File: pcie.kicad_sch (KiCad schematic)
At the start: 9 parts, among them U3 XC7K160T-FFG676

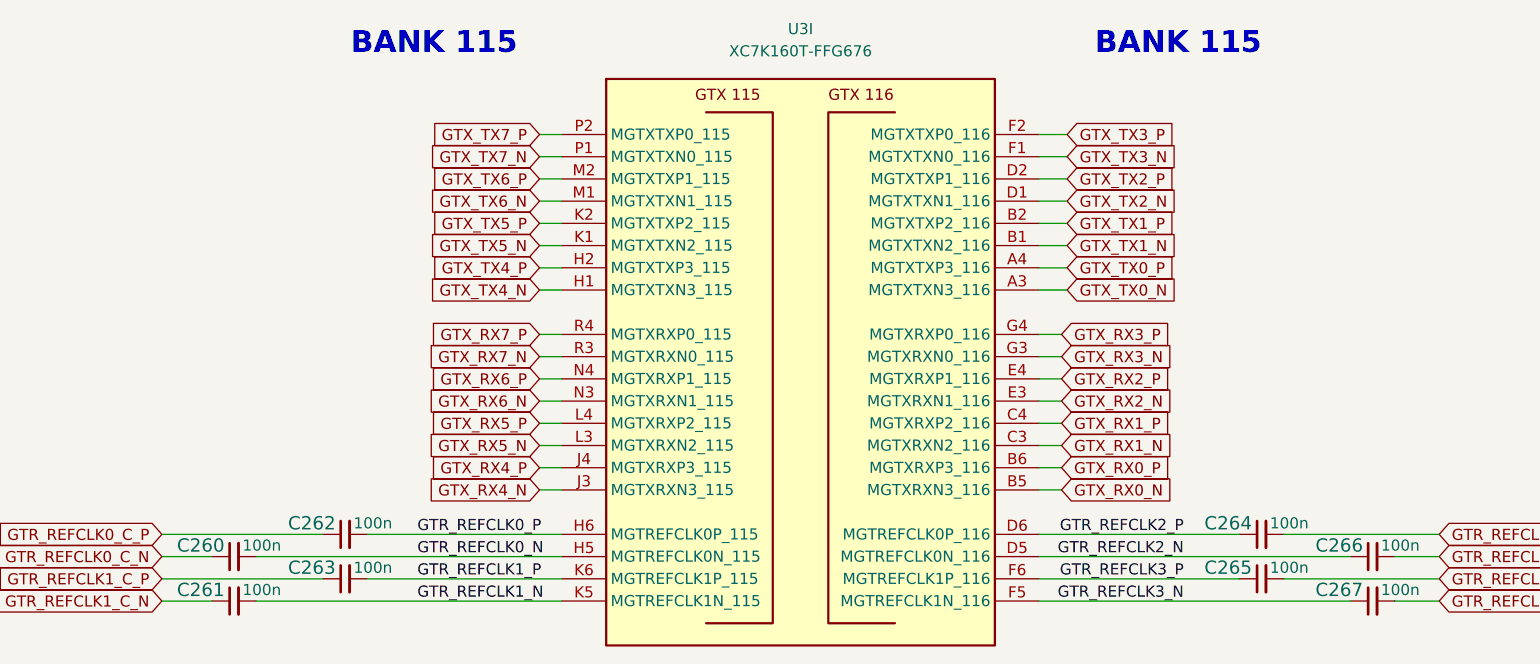
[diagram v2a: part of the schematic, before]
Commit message: Update designators and sync schematic with PCB
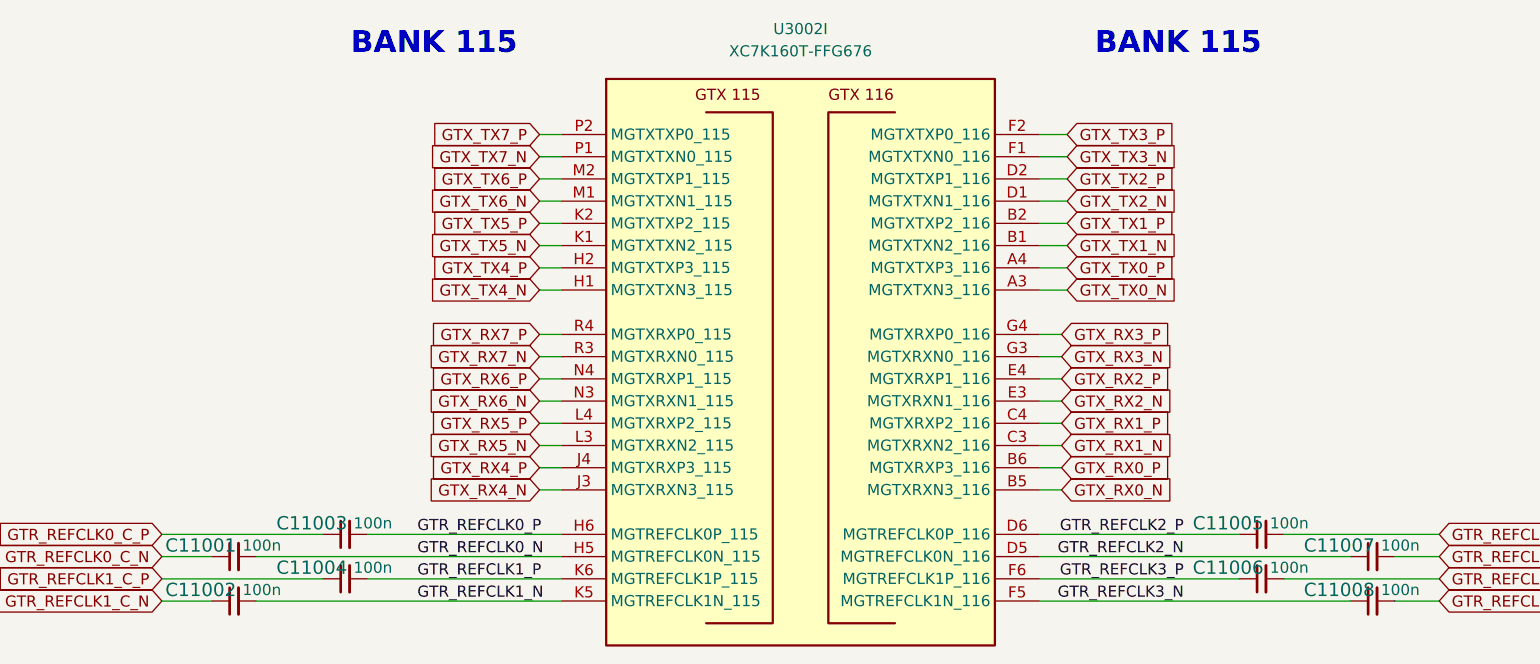
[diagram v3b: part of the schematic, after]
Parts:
- renumbered C260 to C11001, C261 to C11002, C262 to C11003, C263 to C11004, C264 to C11005, C265 to C11006, C266 to C11007, C267 to C11008, U3 to U3002
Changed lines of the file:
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@@
   (symbol (lib_id "data-center-rdimm-ddr4-tester:C_100n_0402") (at 144.78 99.06 0) (unit 1)
     (in_bom yes) (on_board yes)
-    (property "Reference" "C262" (id 0) (at 143.51 97.79 0)
+    (property "Reference" "C11003" (id 0) (at 143.51 97.79 0)
       (effects (font (size 1.524 1.524)))
     )
@@
   (symbol (lib_id "data-center-rdimm-ddr4-tester:C_100n_0402") (at 249.555 104.14 0) (mirror x) (unit 1)
     (in_bom yes) (on_board yes)
-    (property "Reference" "C265" (id 0) (at 248.285 102.87 0)
+    (property "Reference" "C11006" (id 0) (at 248.285 102.87 0)
       (effects (font (size 1.524 1.524)))
     )
@@
   (symbol (lib_id "data-center-rdimm-ddr4-tester:C_100n_0402") (at 132.08 106.68 0) (unit 1)
     (in_bom yes) (on_board yes)
-    (property "Reference" "C261" (id 0) (at 130.81 105.41 0)
+    (property "Reference" "C11002" (id 0) (at 130.81 105.41 0)
       (effects (font (size 1.524 1.524)))
     )
@@
   (symbol (lib_id "data-center-rdimm-ddr4-tester:C_100n_0402") (at 144.78 104.14 0) (unit 1)
     (in_bom yes) (on_board yes)
-    (property "Reference" "C263" (id 0) (at 143.51 102.87 0)
+    (property "Reference" "C11004" (id 0) (at 143.51 102.87 0)
       (effects (font (size 1.524 1.524)))
     )
@@
   (symbol (lib_id "data-center-rdimm-ddr4-tester:C_100n_0402") (at 262.255 101.6 0) (mirror x) (unit 1)
     (in_bom yes) (on_board yes)
-    (property "Reference" "C266" (id 0) (at 260.985 100.33 0)
+    (property "Reference" "C11007" (id 0) (at 260.985 100.33 0)
       (effects (font (size 1.524 1.524)))
     )
@@
   (symbol (lib_id "data-center-rdimm-ddr4-tester:XC7K160T-FFG676") (at 172.085 53.34 0) (unit 9)
     (in_bom yes) (on_board yes) (fields_autoplaced)
-    (property "Reference" "U3" (id 0) (at 199.39 41.275 0))
+    (property "Reference" "U3002" (id 0) (at 199.39 41.275 0))
     (property "Value" "XC7K160T-FFG676" (id 1) (at 199.39 43.815 0)
       (effects (font (size 1.27 1.27) (thickness 0.15)))
@@
   (symbol (lib_id "data-center-rdimm-ddr4-tester:C_100n_0402") (at 262.255 106.68 0) (mirror x) (unit 1)
     (in_bom yes) (on_board yes)
-    (property "Reference" "C267" (id 0) (at 260.985 105.41 0)
+    (property "Reference" "C11008" (id 0) (at 260.985 105.41 0)
       (effects (font (size 1.524 1.524)))
     )
@@
   (symbol (lib_id "data-center-rdimm-ddr4-tester:C_100n_0402") (at 132.08 101.6 0) (unit 1)
     (in_bom yes) (on_board yes)
-    (property "Reference" "C260" (id 0) (at 130.81 100.33 0)
+    (property "Reference" "C11001" (id 0) (at 130.81 100.33 0)
       (effects (font (size 1.524 1.524)))
     )
@@
   (symbol (lib_id "data-center-rdimm-ddr4-tester:C_100n_0402") (at 249.555 99.06 0) (mirror x) (unit 1)
     (in_bom yes) (on_board yes)
-    (property "Reference" "C264" (id 0) (at 248.285 97.79 0)
+    (property "Reference" "C11005" (id 0) (at 248.285 97.79 0)
       (effects (font (size 1.524 1.524)))
     )

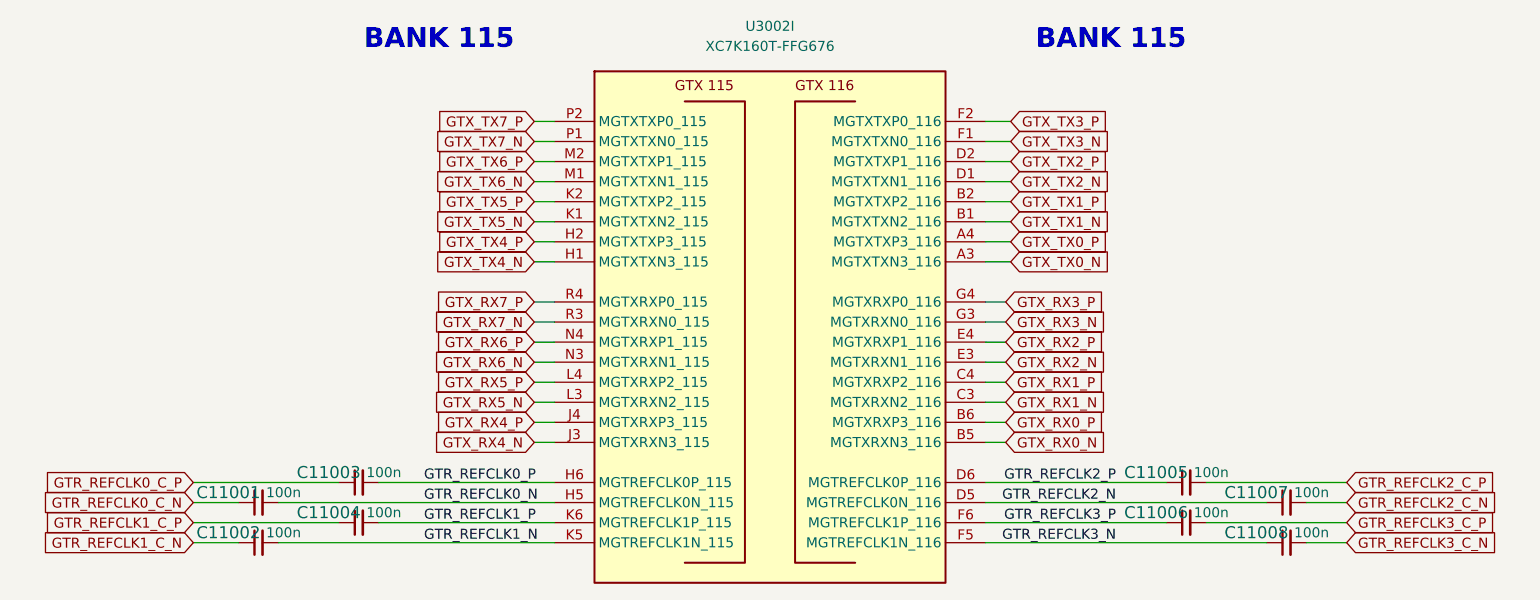
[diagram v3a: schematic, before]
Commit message: Update PCIe connection
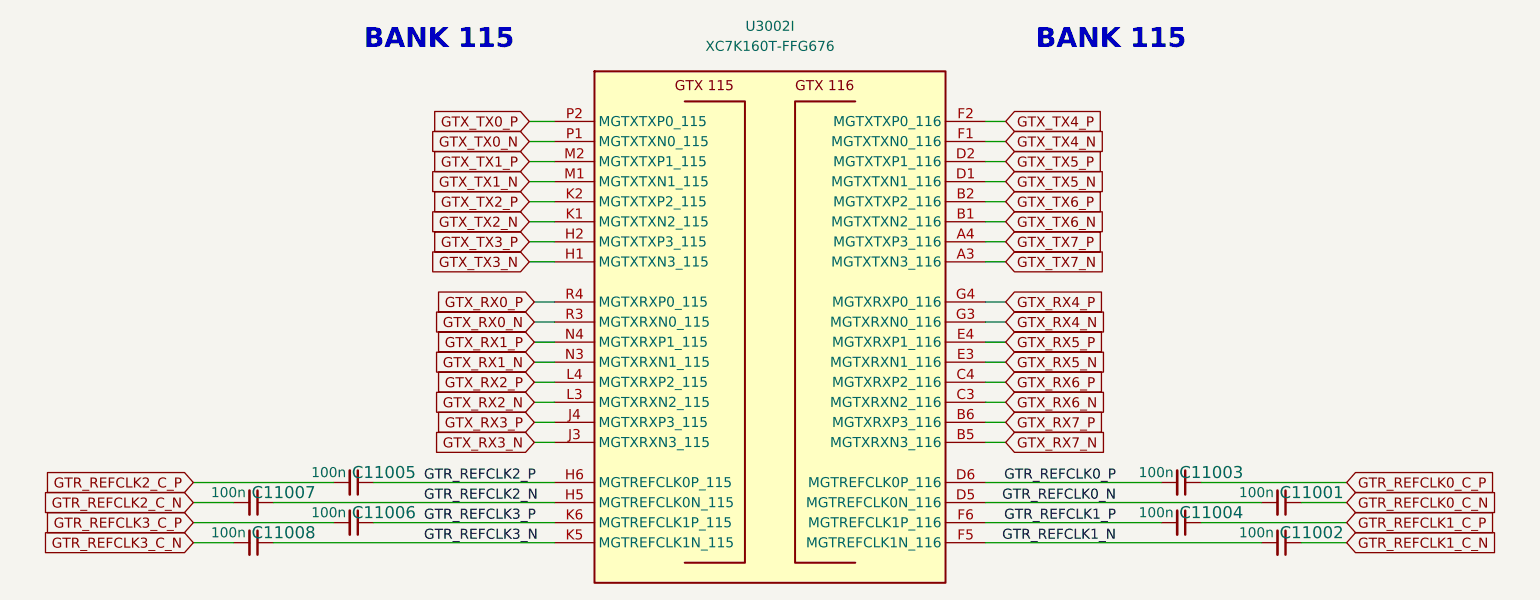
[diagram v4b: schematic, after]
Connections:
- net GTR_REFCLK0_N: now also U3002.D5 (MGTREFCLK0N_116); no longer U3002.H5 (MGTREFCLK0N_115)
- net GTR_REFCLK0_P: now also U3002.D6 (MGTREFCLK0P_116); no longer U3002.H6 (MGTREFCLK0P_115)
- net GTR_REFCLK1_N: now also U3002.F5 (MGTREFCLK1N_116); no longer U3002.K5 (MGTREFCLK1N_115)
- net GTR_REFCLK1_P: now also U3002.F6 (MGTREFCLK1P_116); no longer U3002.K6 (MGTREFCLK1P_115)
- net GTR_REFCLK2_N: now also U3002.H5 (MGTREFCLK0N_115); no longer U3002.D5 (MGTREFCLK0N_116)
- net GTR_REFCLK2_P: now also U3002.H6 (MGTREFCLK0P_115); no longer U3002.D6 (MGTREFCLK0P_116)
- net GTR_REFCLK3_N: now also U3002.K5 (MGTREFCLK1N_115); no longer U3002.F5 (MGTREFCLK1N_116)
- net GTR_REFCLK3_P: now also U3002.K6 (MGTREFCLK1P_115); no longer U3002.F6 (MGTREFCLK1P_116)
- net GTX_RX0_N: now also U3002.R3 (MGTXRXN0_115); no longer U3002.B5 (MGTXRXN3_116)
- net GTX_RX0_P: now also U3002.R4 (MGTXRXP0_115); no longer U3002.B6 (MGTXRXP3_116)
- net GTX_RX1_N: now also U3002.N3 (MGTXRXN1_115); no longer U3002.C3 (MGTXRXN2_116)
- net GTX_RX1_P: now also U3002.N4 (MGTXRXP1_115); no longer U3002.C4 (MGTXRXP2_116)
- net GTX_RX2_N: now also U3002.L3 (MGTXRXN2_115); no longer U3002.E3 (MGTXRXN1_116)
- net GTX_RX2_P: now also U3002.L4 (MGTXRXP2_115); no longer U3002.E4 (MGTXRXP1_116)
- net GTX_RX3_N: now also U3002.J3 (MGTXRXN3_115); no longer U3002.G3 (MGTXRXN0_116)
- net GTX_RX3_P: now also U3002.J4 (MGTXRXP3_115); no longer U3002.G4 (MGTXRXP0_116)
- net GTX_RX4_N: now also U3002.G3 (MGTXRXN0_116); no longer U3002.J3 (MGTXRXN3_115)
- net GTX_RX4_P: now also U3002.G4 (MGTXRXP0_116); no longer U3002.J4 (MGTXRXP3_115)
- net GTX_RX5_N: now also U3002.E3 (MGTXRXN1_116); no longer U3002.L3 (MGTXRXN2_115)
- net GTX_RX5_P: now also U3002.E4 (MGTXRXP1_116); no longer U3002.L4 (MGTXRXP2_115)
- net GTX_RX6_N: now also U3002.C3 (MGTXRXN2_116); no longer U3002.N3 (MGTXRXN1_115)
- net GTX_RX6_P: now also U3002.C4 (MGTXRXP2_116); no longer U3002.N4 (MGTXRXP1_115)
- net GTX_RX7_N: now also U3002.B5 (MGTXRXN3_116); no longer U3002.R3 (MGTXRXN0_115)
- net GTX_RX7_P: now also U3002.B6 (MGTXRXP3_116); no longer U3002.R4 (MGTXRXP0_115)
- net GTX_TX0_N: now also U3002.P1 (MGTXTXN0_115); no longer U3002.A3 (MGTXTXN3_116)
- net GTX_TX0_P: now also U3002.P2 (MGTXTXP0_115); no longer U3002.A4 (MGTXTXP3_116)
- net GTX_TX1_N: now also U3002.M1 (MGTXTXN1_115); no longer U3002.B1 (MGTXTXN2_116)
- net GTX_TX1_P: now also U3002.M2 (MGTXTXP1_115); no longer U3002.B2 (MGTXTXP2_116)
- net GTX_TX2_N: now also U3002.K1 (MGTXTXN2_115); no longer U3002.D1 (MGTXTXN1_116)
- net GTX_TX2_P: now also U3002.K2 (MGTXTXP2_115); no longer U3002.D2 (MGTXTXP1_116)
- net GTX_TX3_N: now also U3002.H1 (MGTXTXN3_115); no longer U3002.F1 (MGTXTXN0_116)
- net GTX_TX3_P: now also U3002.H2 (MGTXTXP3_115); no longer U3002.F2 (MGTXTXP0_116)
- net GTX_TX4_N: now also U3002.F1 (MGTXTXN0_116); no longer U3002.H1 (MGTXTXN3_115)
- net GTX_TX4_P: now also U3002.F2 (MGTXTXP0_116); no longer U3002.H2 (MGTXTXP3_115)
- net GTX_TX5_N: now also U3002.D1 (MGTXTXN1_116); no longer U3002.K1 (MGTXTXN2_115)
- net GTX_TX5_P: now also U3002.D2 (MGTXTXP1_116); no longer U3002.K2 (MGTXTXP2_115)
- net GTX_TX6_N: now also U3002.B1 (MGTXTXN2_116); no longer U3002.M1 (MGTXTXN1_115)
- net GTX_TX6_P: now also U3002.B2 (MGTXTXP2_116); no longer U3002.M2 (MGTXTXP1_115)
- net GTX_TX7_N: now also U3002.A3 (MGTXTXN3_116); no longer U3002.P1 (MGTXTXN0_115)
- net GTX_TX7_P: now also U3002.A4 (MGTXTXP3_116); no longer U3002.P2 (MGTXTXP0_115)
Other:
- moved on the sheet: C11001, C11002, C11003, C11004, C11005, C11006, C11007, C11008

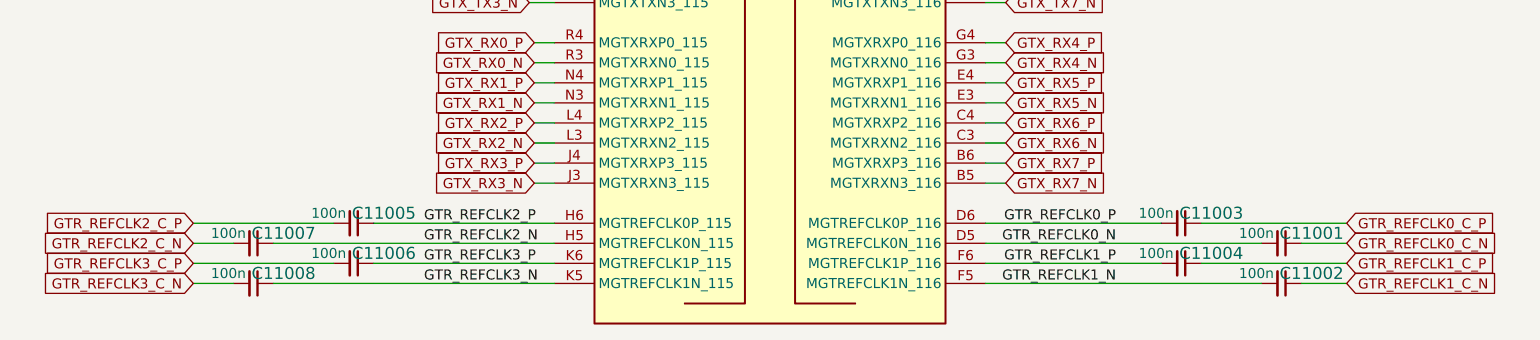
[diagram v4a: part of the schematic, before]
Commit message: Improve DDR assigment, connect ECC to remaining pins, cleanup not used components, continue placement of misc. components
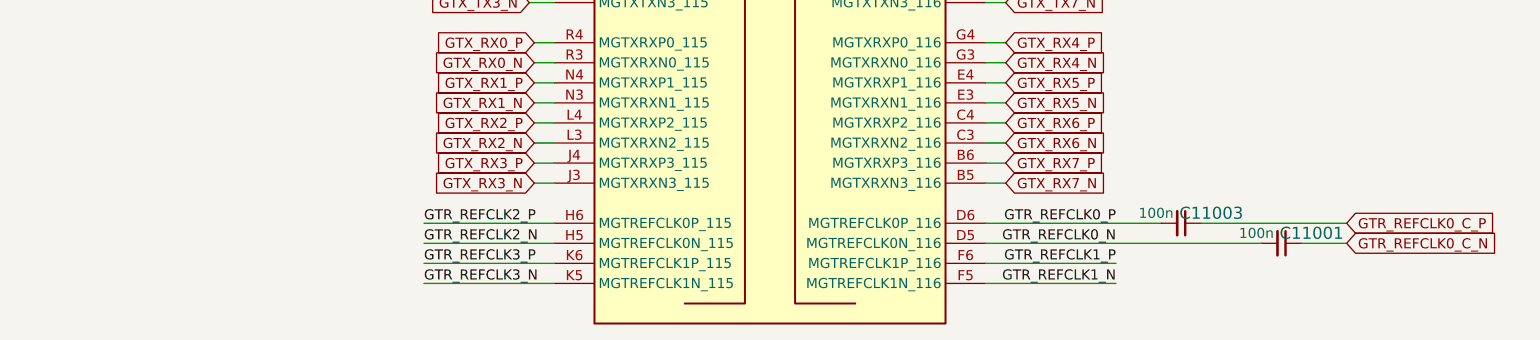
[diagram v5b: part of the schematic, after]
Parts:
- removed C11002, C11004, C11005, C11006, C11007, C11008: C_100n_0402, data-center-rdimm-ddr4-tester-footprints:C_0402_1005Metric, symbol data-center-rdimm-ddr4-tester:C_100n_0402

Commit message: Add loclib
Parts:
- C11001, C11003: footprint data-center-rdimm-ddr4-tester-footprints:C_0402_1005Metric -> sodimm-ddr5-tester-footprints:C_0402_1005Metric; symbol data-center-rdimm-ddr4-tester:C_100n_0402 -> sodimm-ddr5-tester:C_100n_0402
- U3002: footprint data-center-rdimm-ddr4-tester-footprints:BGA-676_27x27mm_Layout26x26_P1X1mm -> sodimm-ddr5-tester-footprints:BGA-676_27x27mm_Layout26x26_P1X1mm; symbol data-center-rdimm-ddr4-tester:XC7K160T-FFG676 -> sodimm-ddr5-tester:XC7K160T-FFG676

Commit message: Bump revision to 1.0.0
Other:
- title: LPDDR5 Test Board -> SO-DIMM DDR5 Tester

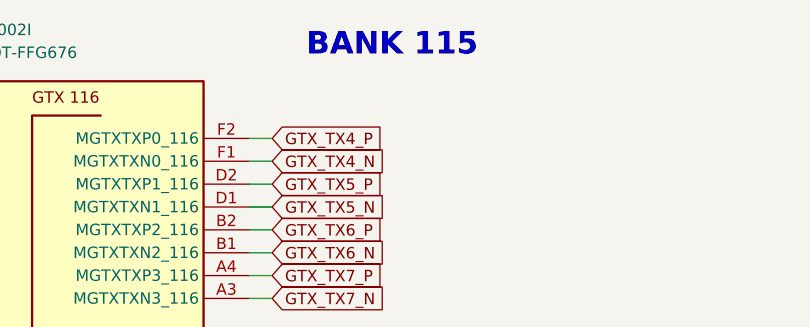
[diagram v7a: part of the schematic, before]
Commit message: Connect control and misc. signals, fix PCIe directions, rework I2C architecture, optimize DC-DC supply utilization
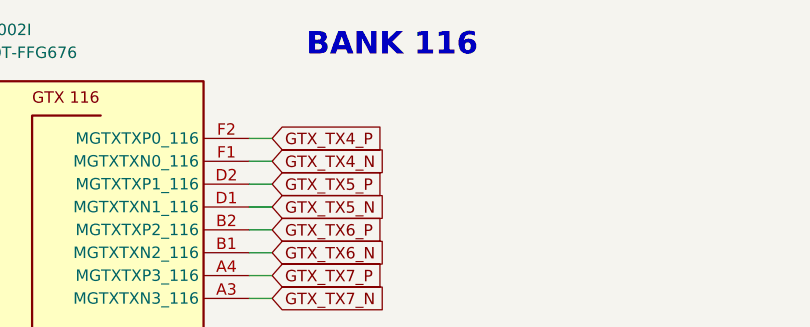
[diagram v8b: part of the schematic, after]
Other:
- note added: "BANK 116"
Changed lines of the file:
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@@
     (effects (font (size 2.4892 2.4892) (thickness 0.4978) bold) (justify left bottom))
   )
-  (text "BANK 115" (at 233.045 44.45 0)
+  (text "BANK 116" (at 233.045 44.45 0)
     (effects (font (size 2.4892 2.4892) (thickness 0.4978) bold) (justify left bottom))
   )
